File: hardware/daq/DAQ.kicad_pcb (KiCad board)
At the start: 2 copper layers, 112 x 120.1 mm, 180 parts, among them J5 ICD26S13E4GX00LF, P1 0022272021, U1 ADS124S08IRHBT, U11 SN74AHCT125RGYR, U2 ADS124S08IRHBT, U3 LT6654BMPS6-5-TRMPBF, U4 LM1086IS-5.0_NOPB, U5 TPS73801DCQR, U6 TPSM63603RDHR, U7 TPSM63603RDHR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

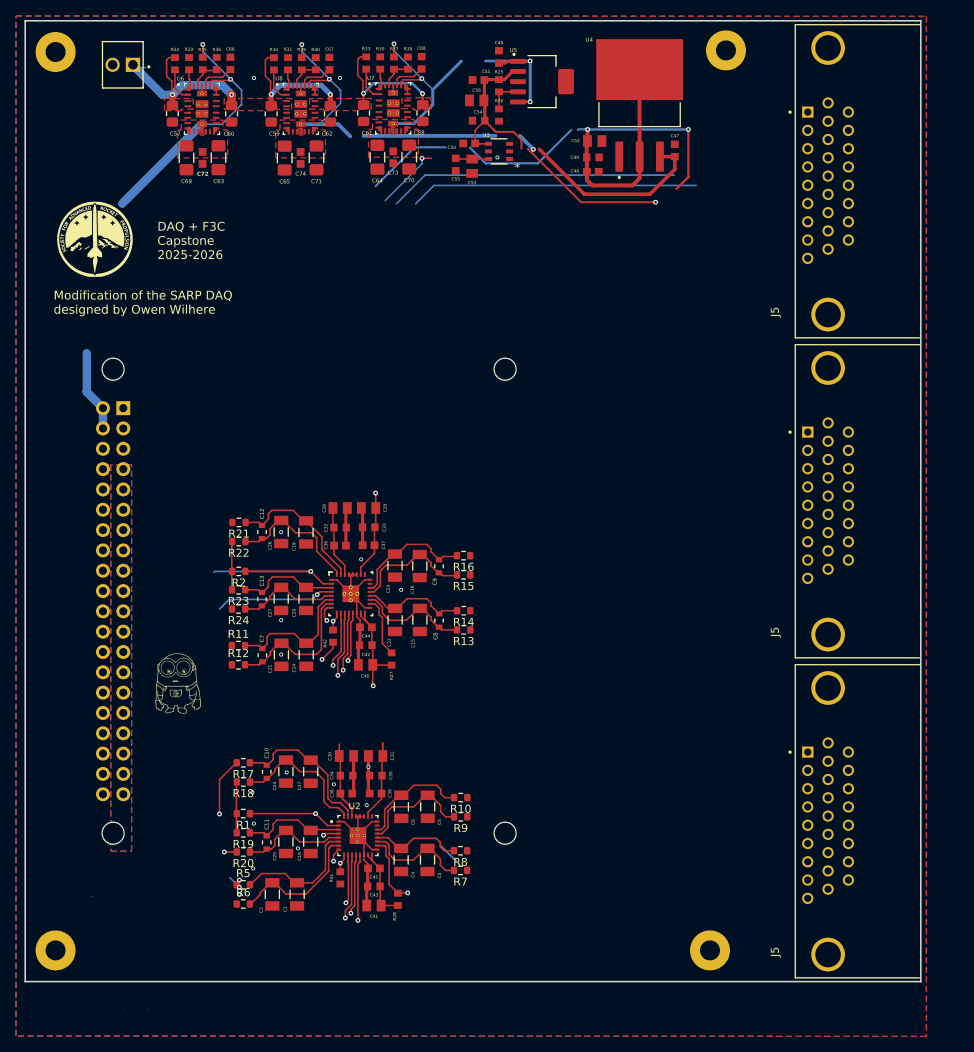
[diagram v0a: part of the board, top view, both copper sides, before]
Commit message: completed 15-pin DSUB pinouts
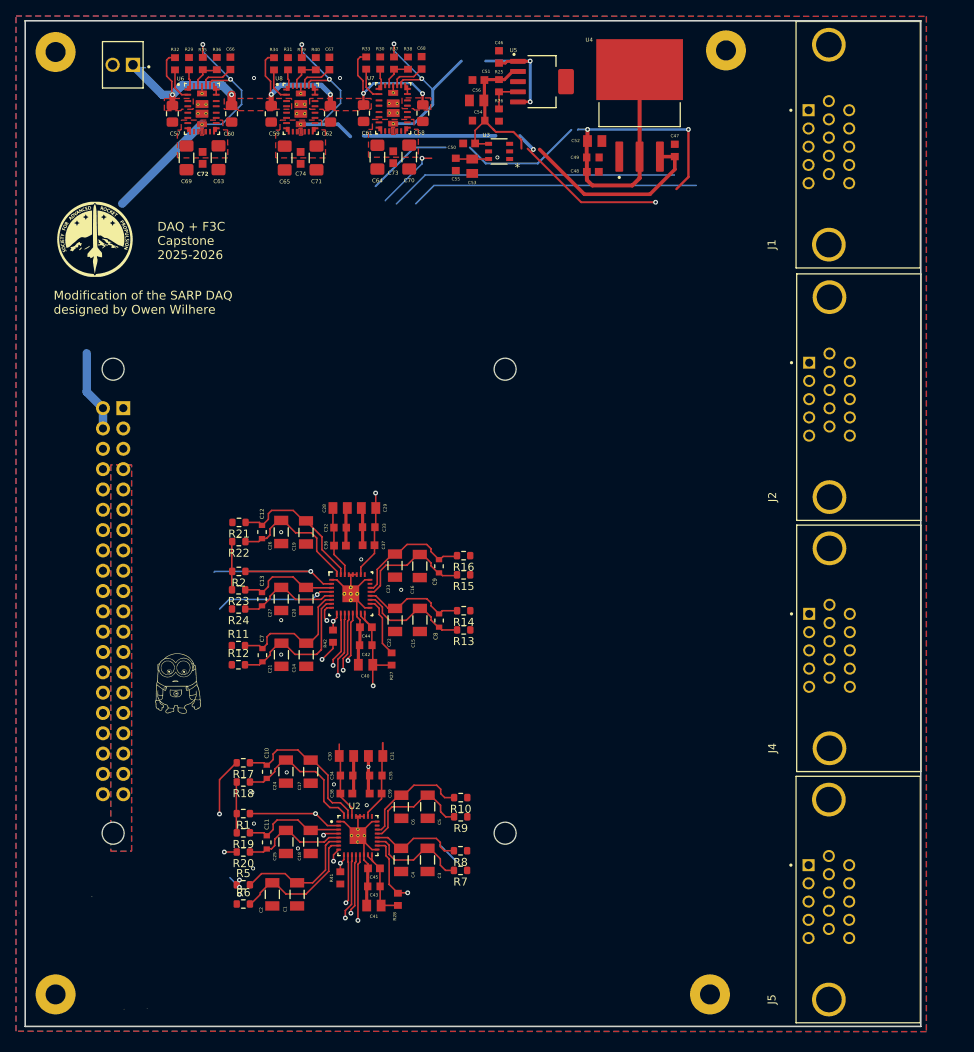
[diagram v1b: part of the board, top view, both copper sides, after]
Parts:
- removed the J5 at (169.0, 128.4)
- removed the J5 at (169.0, 48.4)
- removed the J5 at (169.0, 88.4)
- added J1: ICD15S13E4GX00LF, ICD15S13:AMPHENOL_ICD15S13E4GX00LF, F.Cu at (169.1, 43.8)
- added J2: ICD15S13E4GX00LF, ICD15S13:AMPHENOL_ICD15S13E4GX00LF, F.Cu at (169.1, 75.3)
- added J4: ICD15S13E4GX00LF, ICD15S13:AMPHENOL_ICD15S13E4GX00LF, F.Cu at (169.1, 106.7)
- added J5: ICD15S13E4GX00LF, ICD15S13:AMPHENOL_ICD15S13E4GX00LF, F.Cu at (169.1, 138.1)
- moved H4 5.50 mm to (72.4, 150.0)
- moved H3 5.50 mm to (154.2, 150.0)
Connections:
- D3 pad 4: +5Vs -> /PT3_POW+
- D3 pad 6: +5Vs -> /PT2_POW+
- D4 pad 4: +5Vs -> /PT1_POW+
- D5 pad 6: +5Vs -> /LS3_EXCT+
- D6 pad 4: +5Vs -> /LS2_EXCT+
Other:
- board size 112 x 120.1 mm -> 112 x 125.7 mm

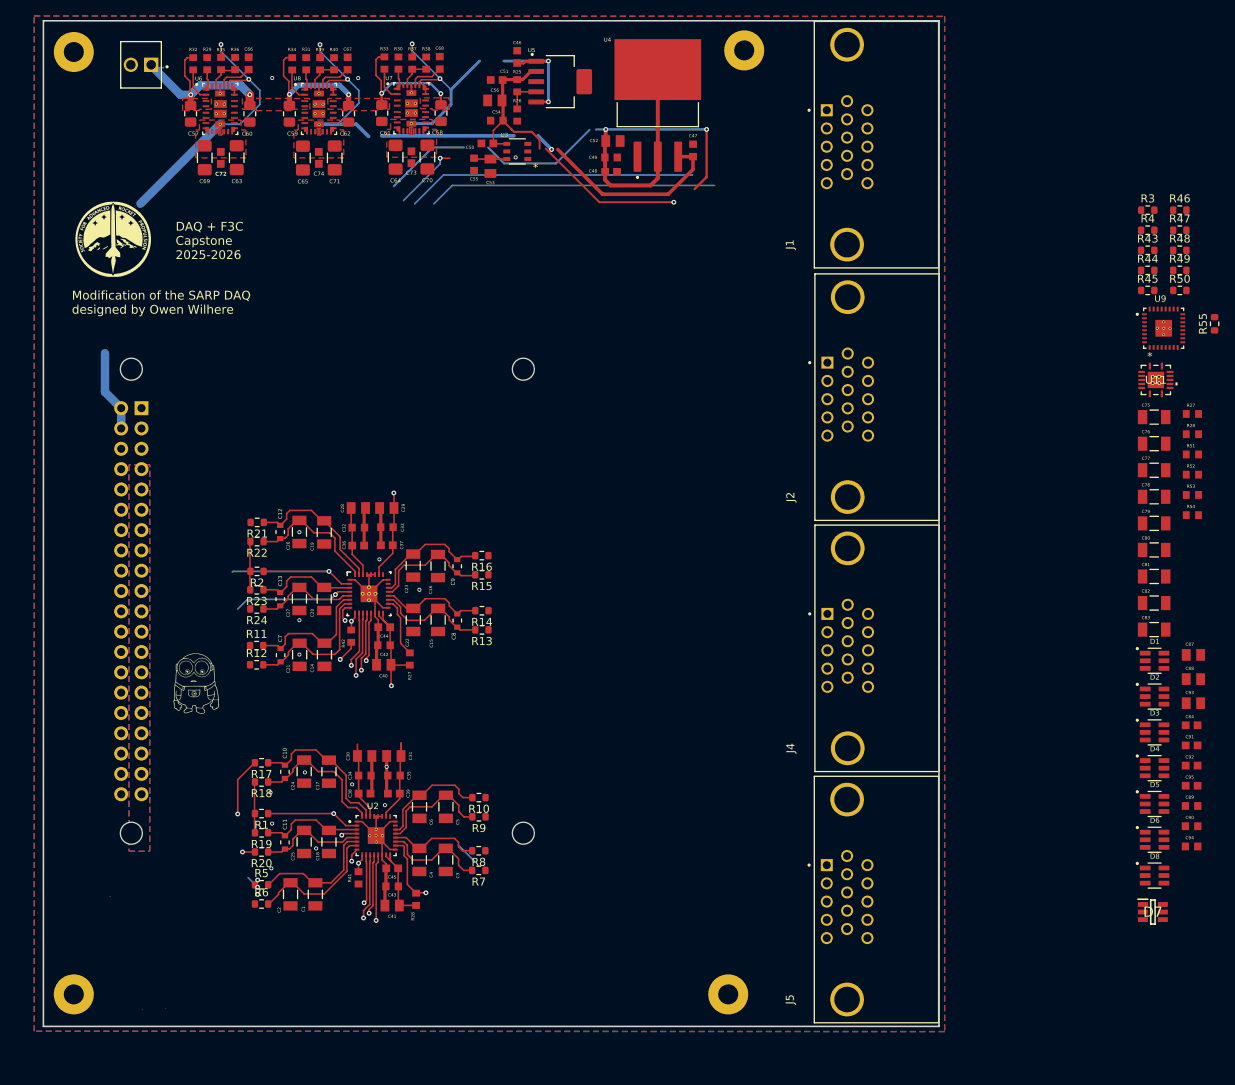
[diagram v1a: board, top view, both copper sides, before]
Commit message: properly dimensioned edge cuts and mounting holes
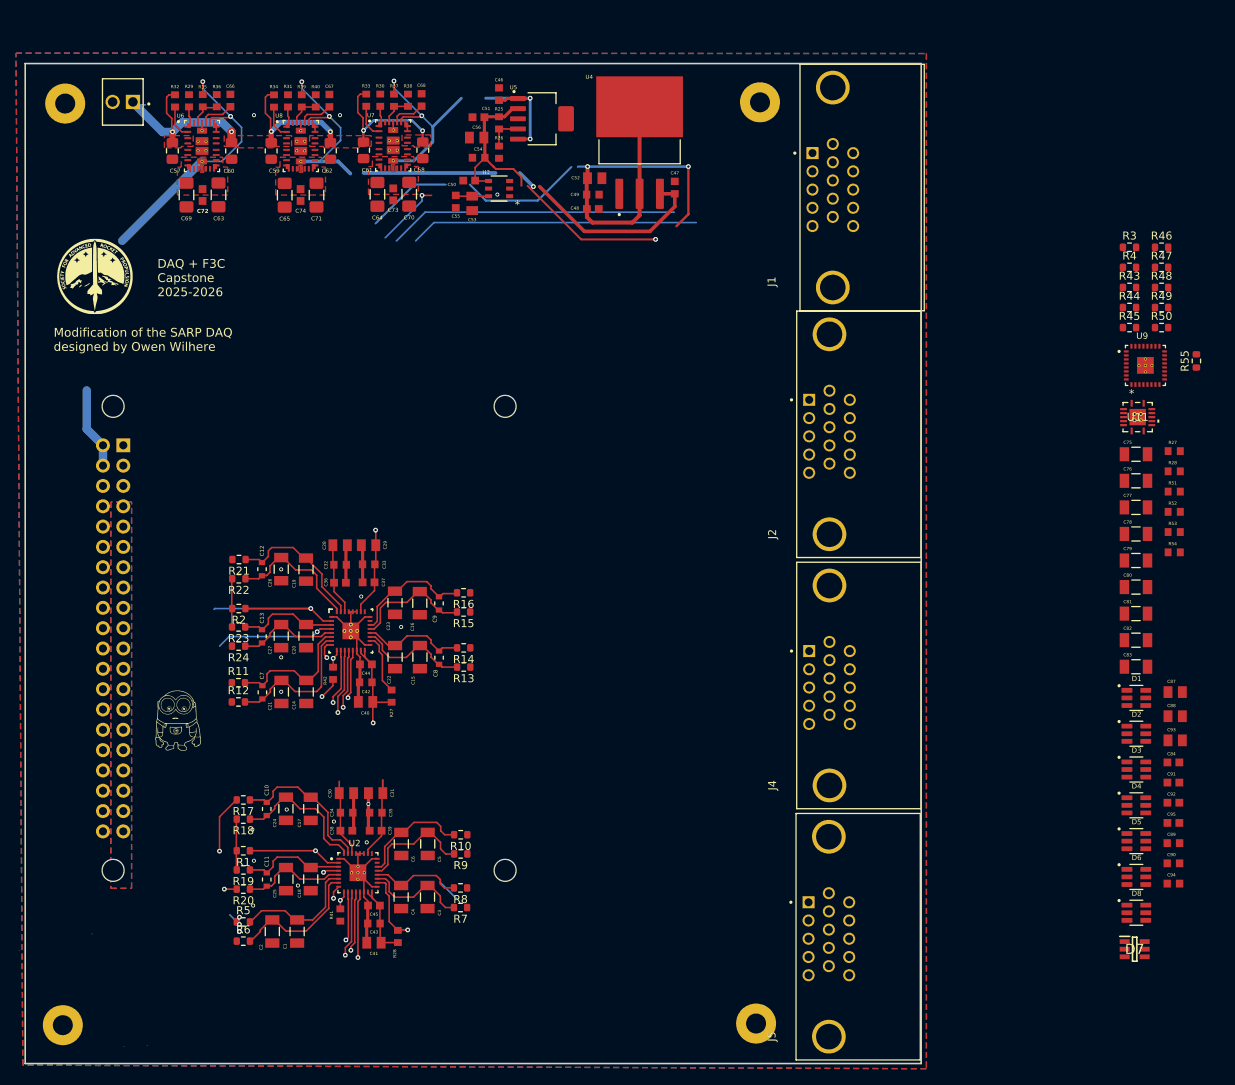
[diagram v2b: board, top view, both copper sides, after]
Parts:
- moved H1 6.78 mm to (158.2, 38.5)
- moved H2 6.53 mm to (71.3, 38.6)
- moved J1 5.65 mm to (167.3, 49.1)
- moved C18 5.17 mm to (102.0, 135.6)
- moved C25 5.17 mm to (98.9, 135.6)
- moved R20 5.17 mm to (93.6, 136.8)
- moved R6 5.17 mm to (93.6, 143.3)
- moved C15 5.17 mm to (115.7, 107.8)
- moved C17 5.17 mm to (102.0, 126.8)
- moved C19 5.17 mm to (101.4, 96.9)
- moved C20 5.17 mm to (101.4, 105.2)
- moved C22 5.17 mm to (112.6, 107.8)
- moved C34 5.17 mm to (106.5, 127.3)
- moved C35 5.17 mm to (110.2, 127.3)
- moved C37 5.17 mm to (109.2, 98.5)
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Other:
- board size 112 x 125.7 mm -> 112 x 125 mm

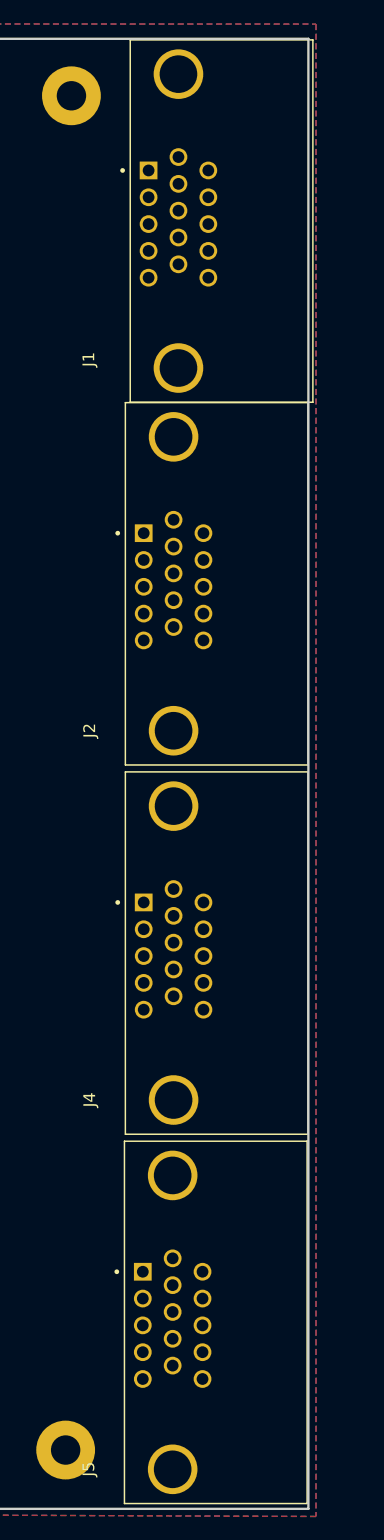
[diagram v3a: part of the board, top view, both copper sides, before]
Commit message: changed stackup to 4 copper layers
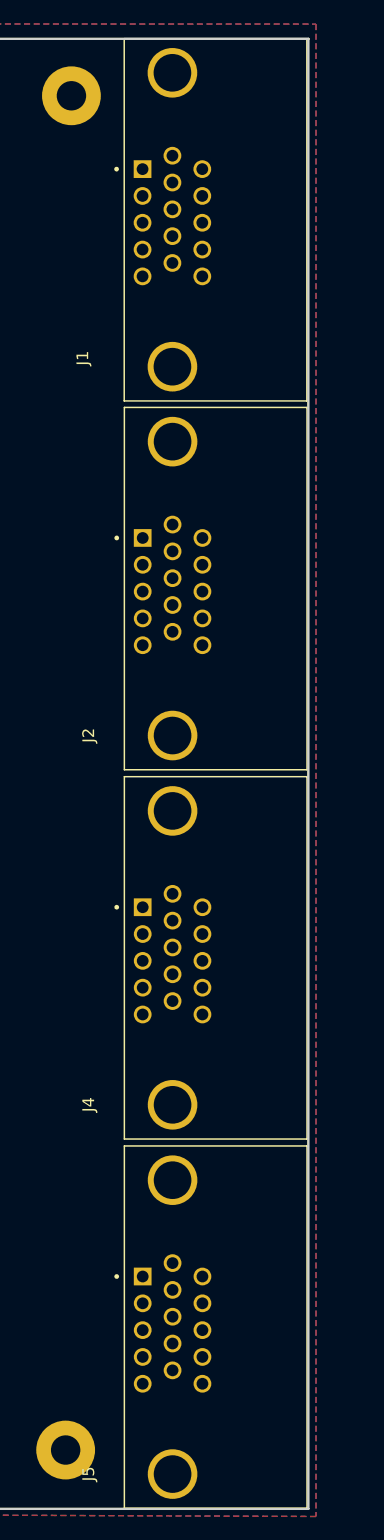
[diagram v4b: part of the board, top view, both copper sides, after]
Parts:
- moved J1 0.52 mm to (166.8, 49.0)
- moved J2 0.42 mm to (166.8, 80.4)
- moved J4 0.42 mm to (166.8, 111.8)
- moved J5 0.40 mm to (166.8, 143.2)
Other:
- copper layers 2 -> 4
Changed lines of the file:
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@@
 	(layers
 		(0 "F.Cu" signal)
+		(4 "In1.Cu" signal)
+		(6 "In2.Cu" signal)
 		(2 "B.Cu" signal)
 		(9 "F.Adhes" user "F.Adhesive")
@@
 	)
 	(setup
+		(stackup
+			(layer "F.SilkS"
+				(type "Top Silk Screen")
+			)
+			(layer "F.Paste"
+				(type "Top Solder Paste")
+			)
+			(layer "F.Mask"
+				(type "Top Solder Mask")
+				(thickness 0.01)
+			)
+			(layer "F.Cu"
+				(type "copper")
+				(thickness 0.035)
+			)
+			(layer "dielectric 1"
+				(type "prepreg")
+				(thickness 0.1)
+				(material "FR4")
+				(epsilon_r 4.5)
+				(loss_tangent 0.02)
+			)
+			(layer "In1.Cu"
+				(type "copper")
+				(thickness 0.035)
+			)
+			(layer "dielectric 2"
+				(type "core")
+				(thickness 1.24)
+				(material "FR4")
+				(epsilon_r 4.5)
+				(loss_tangent 0.02)
+			)
+			(layer "In2.Cu"
+				(type "copper")
+				(thickness 0.035)
+			)
+			(layer "dielectric 3"
+				(type "prepreg")
+				(thickness 0.1)
+				(material "FR4")
+				(epsilon_r 4.5)
+				(loss_tangent 0.02)
+			)
+			(layer "B.Cu"
+				(type "copper")
+				(thickness 0.035)
+			)
+			(layer "B.Mask"
+				(type "Bottom Solder Mask")
+				(thickness 0.01)
+			)
+			(layer "B.Paste"
+				(type "Bottom Solder Paste")
+			)
+			(layer "B.SilkS"
+				(type "Bottom Silk Screen")
+			)
+			(copper_finish "None")
+			(dielectric_constraints no)
+		)
 		(pad_to_mask_clearance 0)
 		(allow_soldermask_bridges_in_footprints no)
@@
 	(footprint "ICD15S13:AMPHENOL_ICD15S13E4GX00LF"
 		(layer "F.Cu")
-		(at 166.86 79.985 90)
+		(at 166.774699 80.392691 90)
 		(property "Reference" "J2"
 			(at -12.48 -7.135 90)
@@
 	(footprint "ICD15S13:AMPHENOL_ICD15S13E4GX00LF"
 		(layer "F.Cu")
-		(at 166.7825 142.78825 90)
+		(at 166.774699 143.192691 90)
 		(property "Reference" "J5"
 			(at -12.48 -7.135 90)
@@
 	(footprint "ICD15S13:AMPHENOL_ICD15S13E4GX00LF"
 		(layer "F.Cu")
-		(at 167.274699 49.142691 90)
+		(at 166.762199 49.029441 90)
 		(property "Reference" "J1"
 			(at -11.765559 -7.627199 90)
@@
 	(footprint "ICD15S13:AMPHENOL_ICD15S13E4GX00LF"
 		(layer "F.Cu")
-		(at 166.86 111.385 90)
+		(at 166.774699 111.792691 90)
 		(property "Reference" "J4"
 			(at -12.48 -7.135 90)

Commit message: updated layout with new ESD components w/ no errors
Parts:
- added C85: 3.3nF, Capacitor_SMD:C_0603_1608Metric_Pad1.08x0.95mm_HandSolder, F.Cu at (232.0, 92.8)
- added C86: 3.3nF, Capacitor_SMD:C_0603_1608Metric_Pad1.08x0.95mm_HandSolder, F.Cu at (232.0, 95.3)
- added C96: 16nF, GRM3195C2A163JA01D:CAPC3216X95N, F.Cu at (232.6, 79.9)
- added C97: 16nF, GRM3195C2A163JA01D:CAPC3216X95N, F.Cu at (232.6, 83.2)
- added C98: 16nF, GRM3195C2A163JA01D:CAPC3216X95N, F.Cu at (232.6, 86.5)
- added C99: 16nF, GRM3195C2A163JA01D:CAPC3216X95N, F.Cu at (232.6, 89.9)
- added D10: ESDA6V1BC6, ESDA6V1BC6:SOT95P280X145-6N, F.Cu at (227.2, 85.0)
- added D11: ESDA6V1BC6, ESDA6V1BC6:SOT95P280X145-6N, F.Cu at (227.2, 89.4)
- added D9: ESDA6V1BC6, ESDA6V1BC6:SOT95P280X145-6N, F.Cu at (227.2, 80.5)
- added R56: 5.6k, Resistor_SMD:R_0603_1608Metric, F.Cu at (222.4, 79.5)
- added R57: 1.8k, Resistor_SMD:R_0603_1608Metric, F.Cu at (222.4, 82.0)
- added R58: 10k, Resistor_SMD:R_0603_1608Metric, F.Cu at (222.4, 84.5)
- added R59: 10k, Resistor_SMD:R_0603_1608Metric, F.Cu at (222.4, 87.0)
- added R60: 10k, Resistor_SMD:R_0603_1608Metric, F.Cu at (222.4, 89.5)
- added R61: 10k, Resistor_SMD:R_0603_1608Metric, F.Cu at (222.4, 92.0)
- C10, C11, C12, C13, C7, C8, C9: footprint footprintsCL10:CAP_CL10_SAM -> Capacitor_SMD:C_0603_1608Metric_Pad1.08x0.95mm_HandSolder
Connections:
- D1 pad 4: unconnected-(D1-Pad4) -> /PT8_SIG
- D1 pad 6: /PT6_POW+ -> /PT7_SIG
- D2 pad 4: /PT5_POW+ -> /PT10_SIG
- D2 pad 6: /PT4_POW+ -> /PT9_SIG
- D3 pad 4: /PT3_POW+ -> /PT12_SIG
- D3 pad 6: /PT2_POW+ -> /PT11_SIG
- D4 pad 4: /PT1_POW+ -> /RTD3_L1
- D5 pad 6: /LS3_EXCT+ -> unconnected-(D5-Pad6)
- D6 pad 4: /LS2_EXCT+ -> +5Vs
- D8 pad 4: unconnected-(D8-Pad4) -> +5Vs
- J1 pad 14: /PT3_SIG -> /RTD3_L3
- J1 pad 4: /PT1_SIG -> /RTD3_L1
- J1 pad 6: /PT2_SIG -> /IDAC2_3
- J4 pad 12: /PT13_SIG -> /PT1_SIG
- J4 pad 13: /PT14_SIG -> /PT2_SIG
- J4 pad 14: /PT15_SIG -> /PT3_SIG
- J5 pad 14: /WTVV -> unconnected-(J5-Pad14)
- J5 pad 6: /PMFV -> unconnected-(J5-Pad6)
- R44 pad 1: /PT14_SIG -> /PT11_SIG
- R45 pad 1: /PT10_SIG -> /PT7_SIG
- R46 pad 1: /PT11_SIG -> /PT8_SIG
- R47 pad 1: /PT12_SIG -> /PT9_SIG
- R48 pad 1: /PT13_SIG -> /PT10_SIG
- R55 pad 1: /PT15_SIG -> /PT12_SIG
- RP1 pad 16: /PWFV -> unconnected-(RP1-GPIO_23-Pad16)
- RP1 pad 3: /FMFV -> /FMV
- RP1 pad 40: /WTVV -> unconnected-(RP1-GPIO21/SPI0_SCLK1-Pad40)
- RP1 pad 5: /OMFV -> /OMV
- U9 pad 2: Net-(U9-AIN5) -> /IDAC1_3
- U9 pad 3: unconnected-(U9-AIN4-Pad3) -> Net-(U9-AIN4)
- U9 pad 31: unconnected-(U9-REFN1_AIN7-Pad31) -> Net-(U9-REFN1_AIN7)
- U9 pad 32: unconnected-(U9-REFP1_AIN6-Pad32) -> Net-(U9-REFP1_AIN6)
- U9 pad 4: Net-(U9-AIN3) -> /IDAC2_3

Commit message: lined up all ESD ICs, need to reorganize ESD/DSUB pins
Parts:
- removed C79, C81, C82: 16nF, GRM3195C2A163JA01D:CAPC3216X95N
- removed R43, R49, R50: 10k, Resistor_SMD:R_0603_1608Metric
- moved C85 251.4 mm to (-19.3, 86.7)
- moved C86 251.4 mm to (-19.3, 89.3)
- moved R44 251.4 mm to (-47.0, 58.1)
- moved R45 251.4 mm to (-47.0, 60.6)
- moved R56 251.4 mm to (-29.0, 73.5)
- moved R57 251.4 mm to (-29.0, 76.0)
- moved R58 251.4 mm to (-29.0, 78.5)
- moved R59 251.4 mm to (-29.0, 81.0)
- moved R60 251.4 mm to (-29.0, 83.5)
- moved R61 251.4 mm to (-29.0, 86.0)
- moved C75 251.4 mm to (-46.2, 76.5)
- moved C76 251.4 mm to (-46.2, 79.8)
- moved C77 251.4 mm to (-46.2, 83.1)
- moved C78 251.4 mm to (-46.2, 86.4)
- moved C80 251.4 mm to (-46.2, 93.1)
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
